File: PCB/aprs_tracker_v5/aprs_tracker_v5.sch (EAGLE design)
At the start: 42 parts, among them IC2 ATMEGA328PB-AUR, IC4 REG1117, T1 2N2222, Y1 ATS080B-E

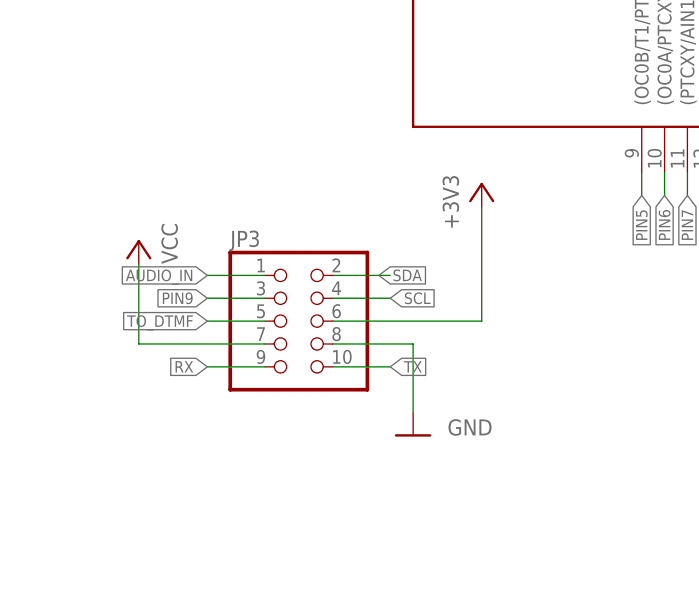
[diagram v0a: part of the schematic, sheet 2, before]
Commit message: added 10k res to the i2c lines
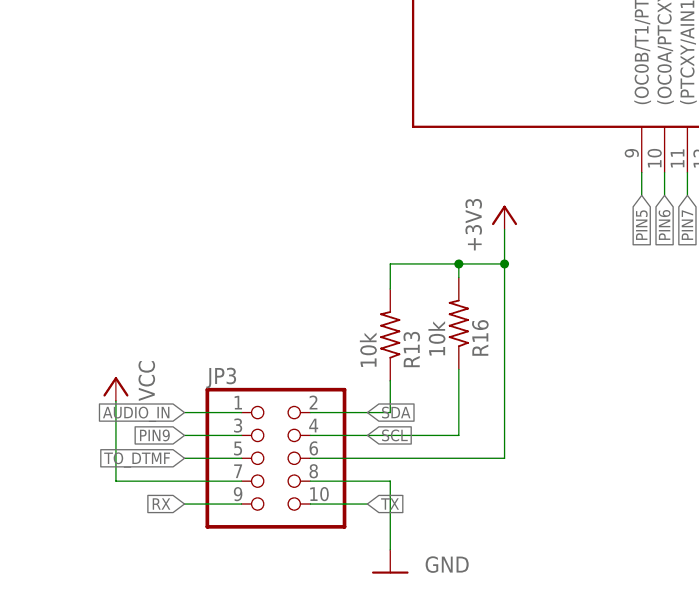
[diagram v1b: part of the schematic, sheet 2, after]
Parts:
- added R13, R16: 10k, rcl:R-US_R0805
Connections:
- net +3V3: now also R13.2, R16.2
- net SCL: now also R16.1
- net SDA: now also R13.1
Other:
- moved on the sheet: JP3
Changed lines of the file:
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@@
 <part name="+3V7" library="supply1" library_urn="urn:adsk.eagle:library:371" deviceset="+3V3" device=""/>
 <part name="C4" library="rcl" library_urn="urn:adsk.eagle:library:334" deviceset="C-US" device="C0805" package3d_urn="urn:adsk.eagle:package:23617/2" value="4.7u"/>
+<part name="R13" library="rcl" library_urn="urn:adsk.eagle:library:334" deviceset="R-US_" device="R0805" package3d_urn="urn:adsk.eagle:package:23553/2" value="10k"/>
+<part name="R16" library="rcl" library_urn="urn:adsk.eagle:library:334" deviceset="R-US_" device="R0805" package3d_urn="urn:adsk.eagle:package:23553/2" value="10k"/>
 </parts>
 <sheets>
@@
 <attribute name="VALUE" x="163.83" y="74.93" size="1.778" layer="96"/>
 </instance>
-<instance part="JP3" gate="A" x="45.72" y="57.15" smashed="yes">
-<attribute name="NAME" x="39.37" y="65.405" size="1.778" layer="95"/>
-<attribute name="VALUE" x="39.37" y="46.99" size="1.778" layer="96"/>
-</instance>
-<instance part="+3V4" gate="G$1" x="67.31" y="72.39" smashed="yes">
-<attribute name="VALUE" x="64.77" y="67.31" size="1.778" layer="96" rot="R90"/>
-</instance>
-<instance part="P+12" gate="VCC" x="29.21" y="66.04" smashed="yes" rot="MR0">
-<attribute name="VALUE" x="31.75" y="63.5" size="1.778" layer="96" rot="MR90"/>
-</instance>
-<instance part="GND14" gate="1" x="59.69" y="44.45" smashed="yes">
-<attribute name="VALUE" x="63.5" y="44.45" size="1.778" layer="96"/>
+<instance part="JP3" gate="A" x="43.18" y="41.91" smashed="yes">
+<attribute name="NAME" x="36.83" y="50.165" size="1.778" layer="95"/>
+<attribute name="VALUE" x="36.83" y="31.75" size="1.778" layer="96"/>
+</instance>
+<instance part="+3V4" gate="G$1" x="69.85" y="69.85" smashed="yes">
+<attribute name="VALUE" x="67.31" y="64.77" size="1.778" layer="96" rot="R90"/>
+</instance>
+<instance part="P+12" gate="VCC" x="26.67" y="50.8" smashed="yes" rot="MR0">
+<attribute name="VALUE" x="29.21" y="48.26" size="1.778" layer="96" rot="MR90"/>
+</instance>
+<instance part="GND14" gate="1" x="57.15" y="29.21" smashed="yes">
+<attribute name="VALUE" x="60.96" y="29.21" size="1.778" layer="96"/>
 </instance>
 <instance part="S2" gate="1" x="160.02" y="180.34" smashed="yes" rot="R270">
@@
 <instance part="+3V7" gate="G$1" x="177.8" y="91.44" smashed="yes">
 <attribute name="VALUE" x="180.34" y="95.25" size="1.778" layer="96" rot="R180"/>
+</instance>
+<instance part="R13" gate="G$1" x="57.15" y="55.626" smashed="yes" rot="MR90">
+<attribute name="NAME" x="58.6486" y="51.816" size="1.778" layer="95" rot="MR90"/>
+<attribute name="VALUE" x="53.848" y="51.816" size="1.778" layer="96" rot="MR90"/>
+</instance>
+<instance part="R16" gate="G$1" x="64.77" y="56.896" smashed="yes" rot="MR90">
+<attribute name="NAME" x="66.2686" y="53.086" size="1.778" layer="95" rot="MR90"/>
+<attribute name="VALUE" x="61.468" y="53.086" size="1.778" layer="96" rot="MR90"/>
 </instance>
 </instances>
@@
 <segment>
 <pinref part="JP3" gate="A" pin="8"/>
-<wire x1="50.8" y1="54.61" x2="59.69" y2="54.61" width="0.1524" layer="91"/>
+<wire x1="48.26" y1="39.37" x2="57.15" y2="39.37" width="0.1524" layer="91"/>
 <pinref part="GND14" gate="1" pin="GND"/>
-<wire x1="59.69" y1="54.61" x2="59.69" y2="46.99" width="0.1524" layer="91"/>
+<wire x1="57.15" y1="39.37" x2="57.15" y2="31.75" width="0.1524" layer="91"/>
 </segment>
 </net>
@@
 <segment>
 <pinref part="P+12" gate="VCC" pin="VCC"/>
-<wire x1="29.21" y1="63.5" x2="29.21" y2="54.61" width="0.1524" layer="91"/>
+<wire x1="26.67" y1="48.26" x2="26.67" y2="39.37" width="0.1524" layer="91"/>
 <pinref part="JP3" gate="A" pin="7"/>
-<wire x1="43.18" y1="54.61" x2="29.21" y2="54.61" width="0.1524" layer="91"/>
+<wire x1="40.64" y1="39.37" x2="26.67" y2="39.37" width="0.1524" layer="91"/>
 </segment>
 </net>
@@
 <segment>
 <pinref part="JP3" gate="A" pin="9"/>
-<wire x1="43.18" y1="52.07" x2="36.83" y2="52.07" width="0.1524" layer="91"/>
-<label x="36.83" y="52.07" size="1.27" layer="95" rot="R180" xref="yes"/>
+<wire x1="40.64" y1="36.83" x2="34.29" y2="36.83" width="0.1524" layer="91"/>
+<label x="34.29" y="36.83" size="1.27" layer="95" rot="R180" xref="yes"/>
 </segment>
 </net>
@@
 <segment>
 <pinref part="JP3" gate="A" pin="10"/>
-<wire x1="50.8" y1="52.07" x2="57.15" y2="52.07" width="0.1524" layer="91"/>
-<label x="57.15" y="52.07" size="1.27" layer="95" xref="yes"/>
+<wire x1="48.26" y1="36.83" x2="54.61" y2="36.83" width="0.1524" layer="91"/>
+<label x="54.61" y="36.83" size="1.27" layer="95" xref="yes"/>
 </segment>
 </net>
@@
 <segment>
 <pinref part="JP3" gate="A" pin="3"/>
-<wire x1="43.18" y1="59.69" x2="36.83" y2="59.69" width="0.1524" layer="91"/>
-<label x="36.83" y="59.69" size="1.27" layer="95" rot="R180" xref="yes"/>
+<wire x1="40.64" y1="44.45" x2="34.29" y2="44.45" width="0.1524" layer="91"/>
+<label x="34.29" y="44.45" size="1.27" layer="95" rot="R180" xref="yes"/>
 </segment>
 </net>
@@
 <segment>
 <pinref part="JP3" gate="A" pin="4"/>
-<wire x1="50.8" y1="59.69" x2="57.15" y2="59.69" width="0.1524" layer="91"/>
-<label x="57.15" y="59.69" size="1.27" layer="95" xref="yes"/>
+<label x="54.61" y="44.45" size="1.27" layer="95" xref="yes"/>
+<wire x1="48.26" y1="44.45" x2="64.77" y2="44.45" width="0.1524" layer="91"/>
+<pinref part="R16" gate="G$1" pin="1"/>
+<wire x1="64.77" y1="44.45" x2="64.77" y2="51.816" width="0.1524" layer="91"/>
 </segment>
 </net>
@@
 <segment>
 <pinref part="JP3" gate="A" pin="2"/>
-<wire x1="50.8" y1="62.23" x2="57.15" y2="62.23" width="0.1524" layer="91"/>
-<label x="55.88" y="62.23" size="1.27" layer="95" xref="yes"/>
+<wire x1="48.26" y1="46.99" x2="53.34" y2="46.99" width="0.1524" layer="91"/>
+<label x="54.61" y="46.99" size="1.27" layer="95" xref="yes"/>
+<pinref part="R13" gate="G$1" pin="1"/>
+<wire x1="53.34" y1="46.99" x2="54.61" y2="46.99" width="0.1524" layer="91"/>
+<wire x1="57.15" y1="50.546" x2="57.15" y2="46.99" width="0.1524" layer="91"/>
+<wire x1="57.15" y1="46.99" x2="54.61" y2="46.99" width="0.1524" layer="91"/>
 </segment>
 </net>
@@
 <segment>
 <pinref part="+3V4" gate="G$1" pin="+3V3"/>
-<wire x1="67.31" y1="69.85" x2="67.31" y2="57.15" width="0.1524" layer="91"/>
+<wire x1="69.85" y1="67.31" x2="69.85" y2="63.5" width="0.1524" layer="91"/>
 <pinref part="JP3" gate="A" pin="6"/>
-<wire x1="67.31" y1="57.15" x2="50.8" y2="57.15" width="0.1524" layer="91"/>
+<wire x1="69.85" y1="63.5" x2="69.85" y2="41.91" width="0.1524" layer="91"/>
+<wire x1="69.85" y1="41.91" x2="48.26" y2="41.91" width="0.1524" layer="91"/>
+<pinref part="R13" gate="G$1" pin="2"/>
+<wire x1="57.15" y1="60.706" x2="57.15" y2="63.5" width="0.1524" layer="91"/>
+<wire x1="57.15" y1="63.5" x2="64.77" y2="63.5" width="0.1524" layer="91"/>
+<pinref part="R16" gate="G$1" pin="2"/>
+<wire x1="64.77" y1="63.5" x2="64.77" y2="61.976" width="0.1524" layer="91"/>
+<wire x1="64.77" y1="63.5" x2="69.85" y2="63.5" width="0.1524" layer="91"/>
+<junction x="64.77" y="63.5"/>
+<junction x="69.85" y="63.5"/>
 </segment>
 <segment>
@@
 <segment>
 <pinref part="JP3" gate="A" pin="5"/>
-<wire x1="43.18" y1="57.15" x2="36.83" y2="57.15" width="0.1524" layer="91"/>
-<label x="36.83" y="57.15" size="1.27" layer="95" rot="R180" xref="yes"/>
+<wire x1="40.64" y1="41.91" x2="34.29" y2="41.91" width="0.1524" layer="91"/>
+<label x="34.29" y="41.91" size="1.27" layer="95" rot="R180" xref="yes"/>
 </segment>
 </net>
@@
 <segment>
 <pinref part="JP3" gate="A" pin="1"/>
-<wire x1="43.18" y1="62.23" x2="36.83" y2="62.23" width="0.1524" layer="91"/>
-<label x="36.83" y="62.23" size="1.27" layer="95" rot="R180" xref="yes"/>
-</segment>
-</net>
+<wire x1="40.64" y1="46.99" x2="34.29" y2="46.99" width="0.1524" layer="91"/>
+<label x="34.29" y="46.99" size="1.27" layer="95" rot="R180" xref="yes"/>
+</segment>
+</net>

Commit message: added v5 final production PCB
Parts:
- removed D1: (no value), led:LEDCHIP-LED0805
- removed R15: 1k, rcl:R-US_R0805
- added D2: (no value), led:LEDCHIP-LED0805
- added IC3: 74LVCH1T45GW,125, 74LVCH1T45GW_125:74LVCH1T45GW,125
- added R17: 1k, rcl:R-US_R0805
- PWR_IN: value (none) -> PINHD-1X2; device pinhead:PINHD-1X2 -> Connector:PINHD-1X2
- X1: value (none) -> BU-SMA-V; device pinhead:PINHD-1X2 -> con-coax:BU-SMA-V
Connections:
- removed net AUDIO_IN: JP3.1
- removed net N$3: D1.C, R15.2
- new net N$1: IC3.B, U1.TX
- new net N$9: D2.C, R17.2
- net +3V3: now also IC3.VCC(B); no longer D1.A, IC2.(SCL1/T4/PTCXY)_PE1, IC2.AVCC, IC2.VCC, JP1.5, JP3.6, R13.2, R16.2, R6.2
- net GND: now also IC3.DIR, IC3.GND
- net GPS_RX: now also IC3.A, R17.1; no longer R15.1, U1.TX
- net MC_APRS_OUT: now also JP3.1
- net VCC: now also D2.A, IC2.(SCL1/T4/PTCXY)_PE1, IC2.AVCC, IC2.VCC, IC3.VCC(A), JP1.5, JP3.6, R13.2, R16.2, R6.2
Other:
- note added: "B to A : DIR low"
- moved on the sheet: D3, PWR_IN, R12, U1
